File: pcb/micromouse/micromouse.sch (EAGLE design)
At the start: 57 parts, among them J1 Connector_M1, J2 Connector_M2, J4 Programmer

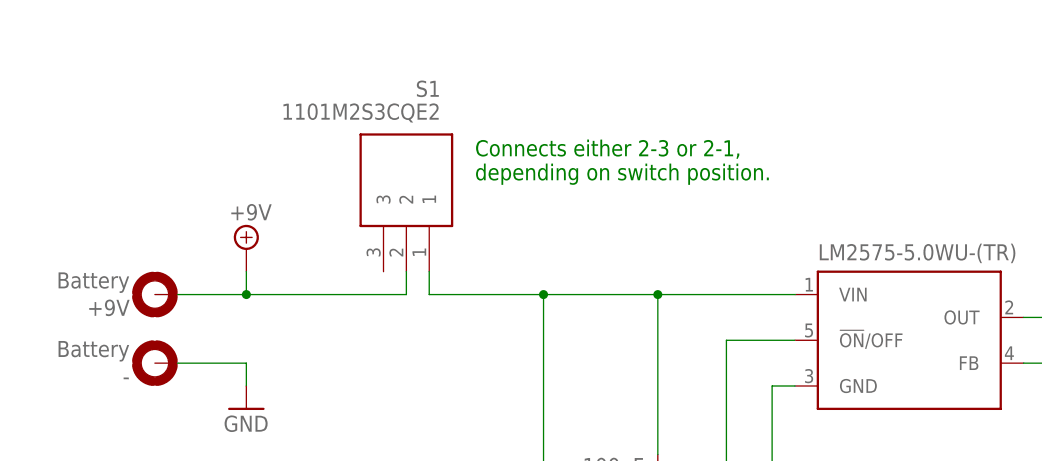
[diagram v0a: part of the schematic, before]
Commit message: Fix positioning of power switch.
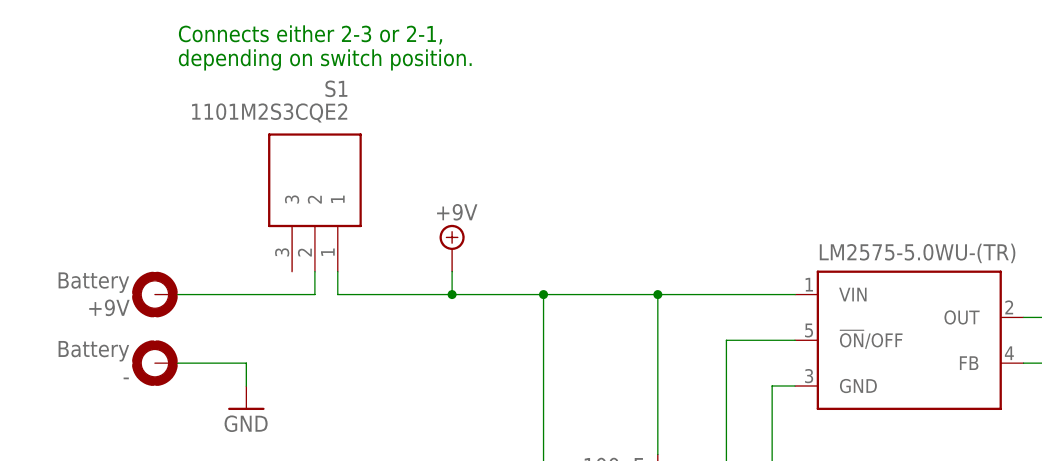
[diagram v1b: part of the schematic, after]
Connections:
- removed net N$3: C12.2, C14.2, LM2575-3.3WU-(TR).VIN, LM2575-5.0WU-(TR).VIN, S1.1
- new net N$2: +9V.MOUNT, S1.2
- net +9V: now also C12.2, C14.2, LM2575-3.3WU-(TR).VIN, LM2575-5.0WU-(TR).VIN, S1.1; no longer +9V.MOUNT, S1.2
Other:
- moved on the sheet: S1

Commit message: Remove resolved comments and only use resistors fom E12 series.
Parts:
- R10, R11, R12: value 121 -> 120R
- R13, R14: value 10 -> 10R
- R3, R4, R8: value 10k -> 10kR
- R9: value 1k -> 1kR
- renumbered HC05/06 to HC05
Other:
- note added: "Use socket instead of soldering the chip directly onto the board."
- note added: "p. 357 datasheet of uC: max. output current of uC = 15mA."
- note removed: "2.54mm grid needed according to motor data sheet (this conector fulfills this: https://www.mikrocontroller.net/topic/393245)"
- note removed: "Add jumper to disconnect them from pins on uC in case we need the pins later on (like on demo board)? >>> No, we have enough pins on the board."
- note removed: "IDEA: Coupling capacitor?"
- note removed: "IDEA: Should we use 3.3V instead since our digital logic is 3.3V as well? Worried that this wiill lead to 5V in the encoder output that then routes into the microcontroller. >>> Good point, cannot hurt."
- note removed: "IDEA: Use one of these holders instead of soldering the chip directly onto the board"
- note removed: "MCLR needs to be negated for the programmer? >>>See p.8 of microcontroller datasheet: 0 equals to reset? This is what reset button does."
- note removed: "PIN6 EN nutzen? >>> Sehe jetzt keine Notwendigkeit. Das Setup mit den AT commands können wir ha auf dem Breadboard machen."
- note removed: "TODO: Ask Lenz if external components are correct"
- note removed: "TODO: Check if these are the correct ones. Seems to me that we need 1.5mm pin distances: https://www.datasheets.com/en/part-details/11501w00-3p-s-hf-r-shenglan-technology-co---ltd-403414635 Are female or male headers needed?"
- note removed: "TODO: Please check PGD and PGC. I think that PGD is on 4 and PGC on 5. >>> Yes, changed it. TODO 2: Why are on the demo board not the signals PGEC1 and PGED1 used but the outputs of pins 11 & 12?"
- note removed: "TODO: S. 357 Microcontroller: Anscheinend haben unterschiedliche PINS unterschiedliche max. Strombegrenzung. Checken dass PINS 20mA liefern können. Zusätzlich 200mA max auf allen PINs. >>> Solution: Draw current diretly from power source (switching regulator)"
- note removed: "TODO: Where do we need decoupling capacitors?"

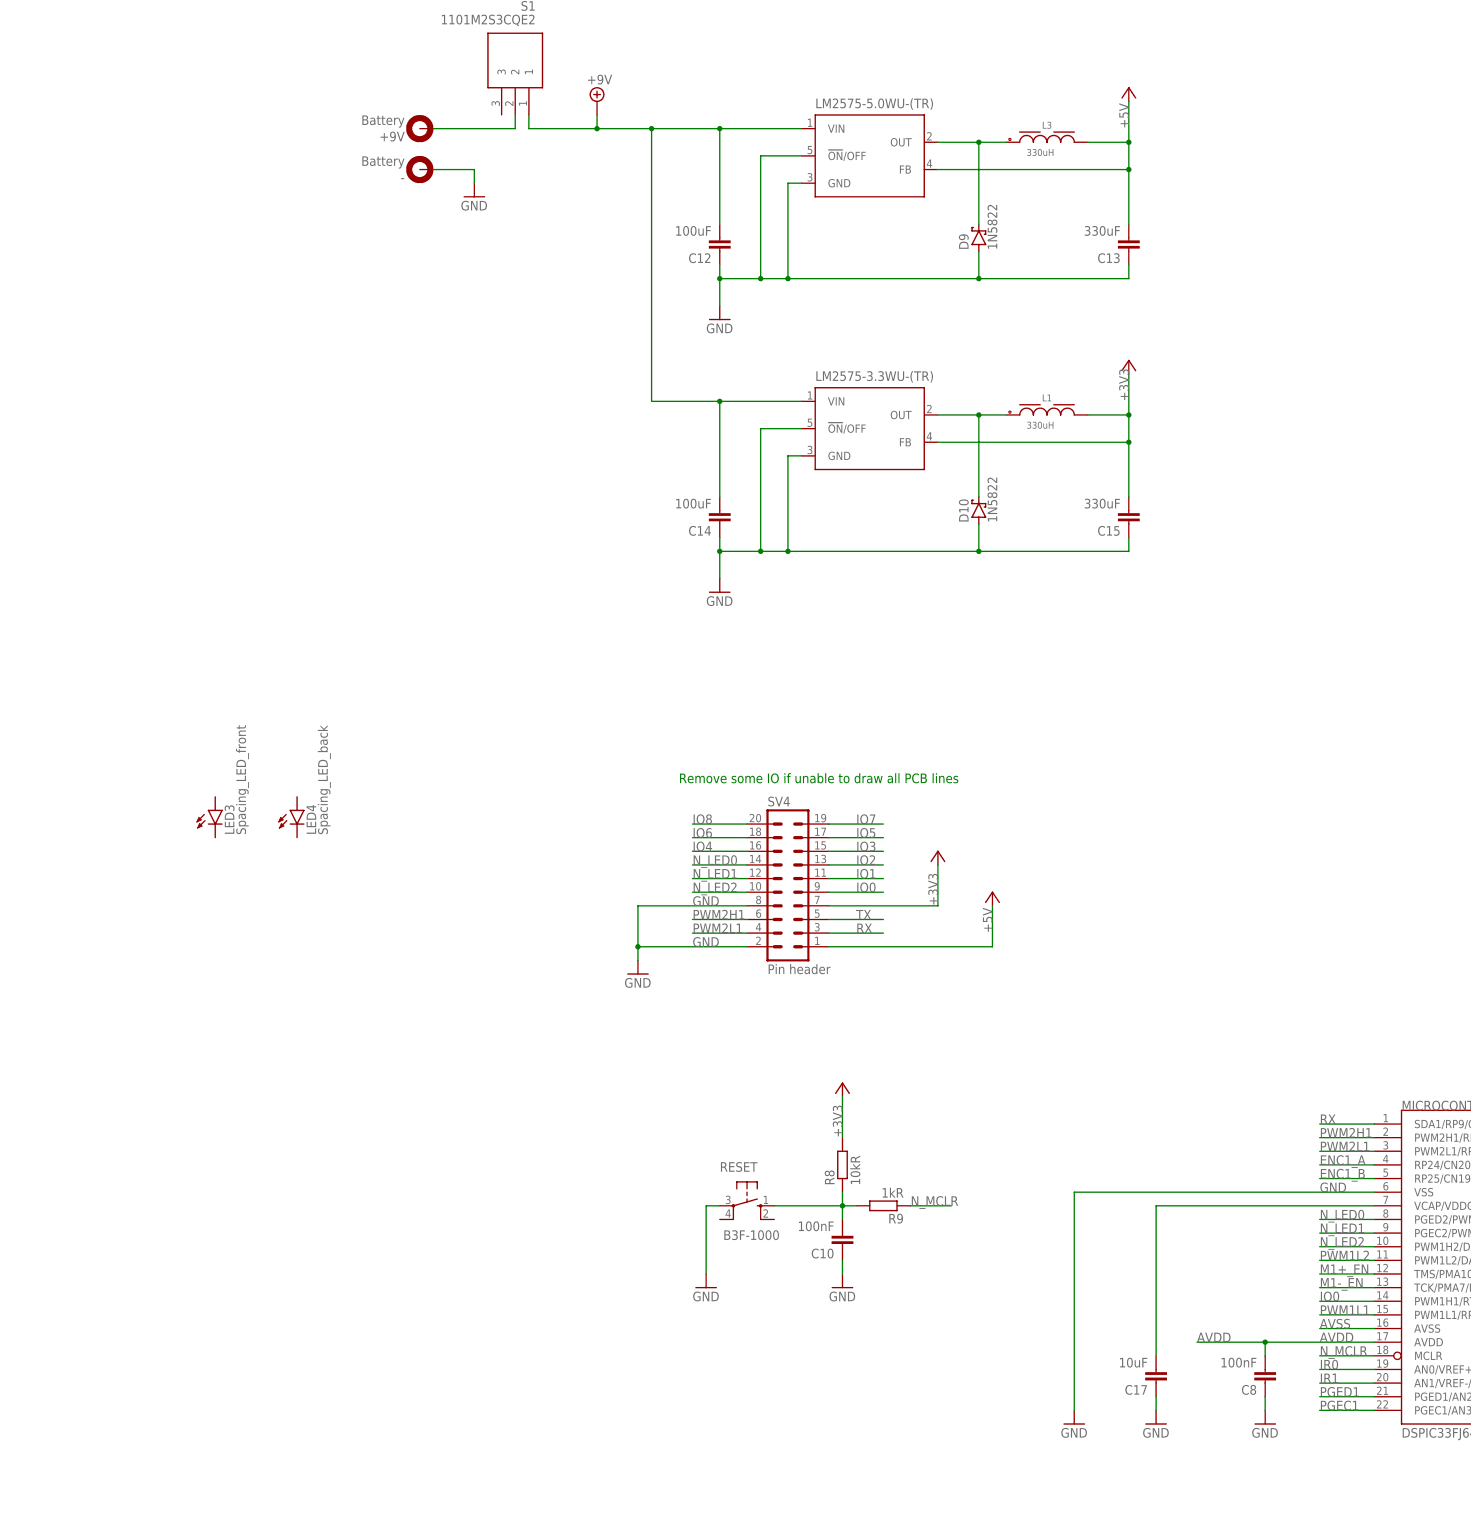
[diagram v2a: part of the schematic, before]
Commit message: Use pin header as battery connector and change reset botton setup.
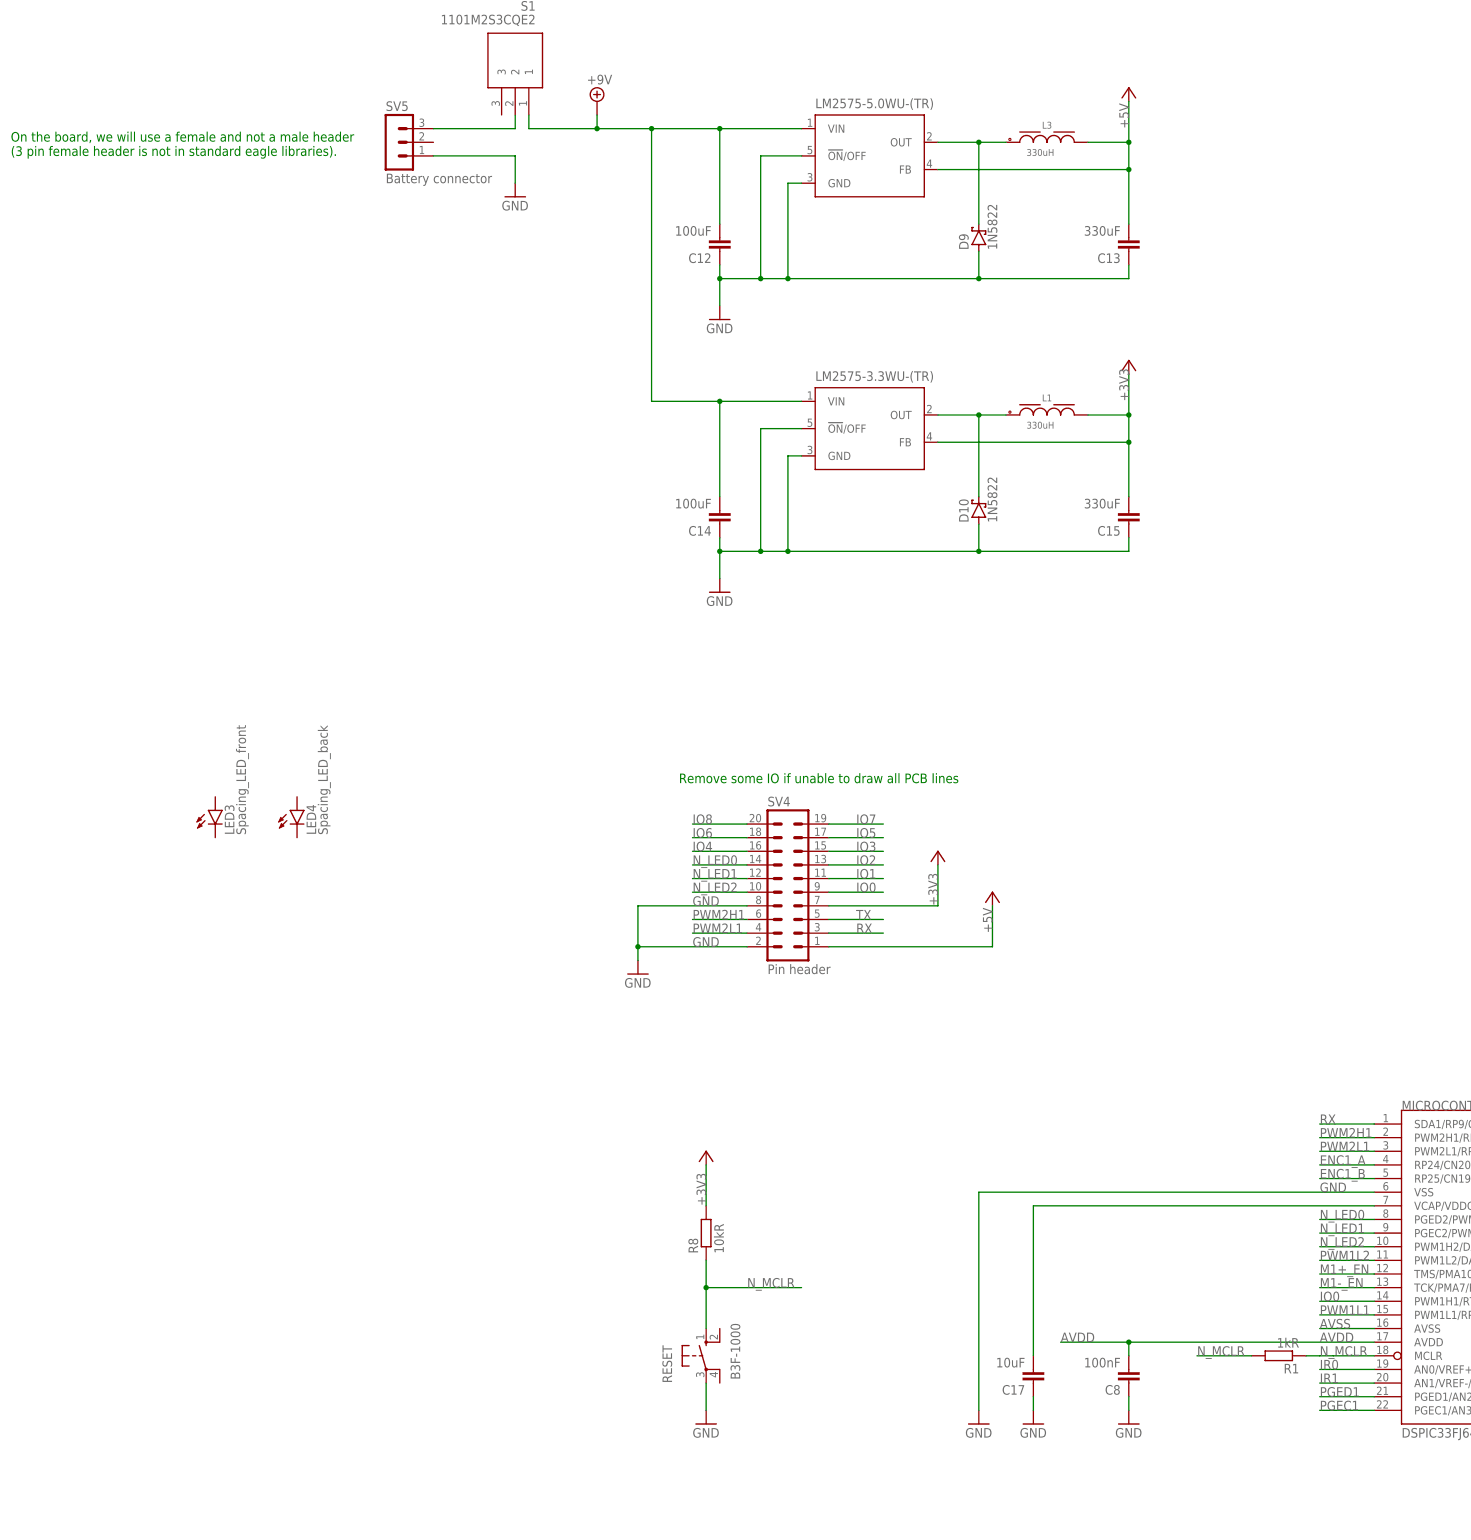
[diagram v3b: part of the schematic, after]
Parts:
- removed +9V, -: Battery, holes:MOUNT-PAD-ROUND3.0
- removed C10: 100nF, rcl:C-EUC0805
- removed R9: 1kR, rcl:R-EU_R0805
- added R1: 1kR, rcl:R-EU_R0805
- added SV5: Battery connector, con-lstb:MA03-1
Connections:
- removed net N$1: C10.2, R8.1, R9.2, RESET.S
- net GND: now also SV5.1; no longer -.MOUNT, C10.1
- net N$2: now also SV5.3; no longer +9V.MOUNT
- net N_MCLR: now also R1.1, R1.2, R8.1, RESET.S; no longer R9.1
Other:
- note added: "On the board, we will use a female and not a male header (3 pin female header is not in standard eagle libraries)."
- moved on the sheet: C17, C8, R8, RESET

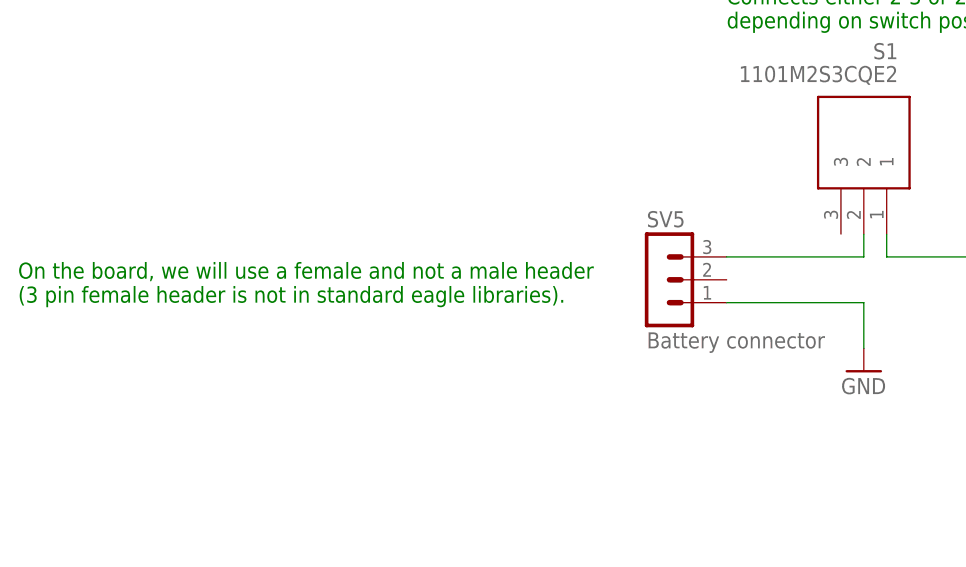
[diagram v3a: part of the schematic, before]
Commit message: Removed comment at battery connector. We will use a male one on the board
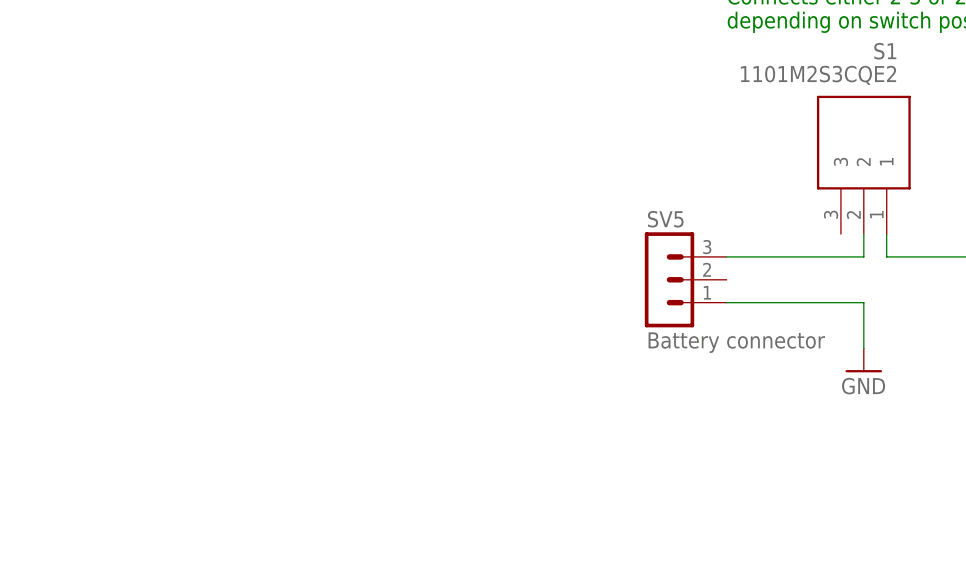
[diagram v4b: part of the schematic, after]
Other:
- note removed: "On the board, we will use a female and not a male header (3 pin female header is not in standard eagle libraries)."
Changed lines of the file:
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@@
 depending on switch position.</text>
 <text x="-58.42" y="223.52" size="1.778" layer="91">Remove some IO if unable to draw all PCB lines</text>
-<text x="-182.88" y="340.36" size="1.778" layer="91">On the board, we will use a female and not a male header
-(3 pin female header is not in standard eagle libraries).</text>
 </plain>
 <instances>
